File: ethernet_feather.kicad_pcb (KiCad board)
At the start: 4 copper layers, 100 parts, among them J1 JST PH 2 pin, J2 JST SH4 pin, J3 Molex 1051620001, J4 TC2030-NL, J5 USB_C_Receptacle_USB2.0, J6 RJ45_Abracon_ARJM11D7-114-AB-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, J7 2x2 header, Q1 Q_PMOS_DGS, U1 MIMXRT1051CVJ5B, U2 LP3982IMM-3.3, U3 MCP73831-2-OT, U4 W25Q32JVZP, U5 WE-TVS-82400102, U6 LAN8742A, U7 HSP061-4M10, Y1 32.768kHz, Y2 24MHz 6pF, Y3 25MHz

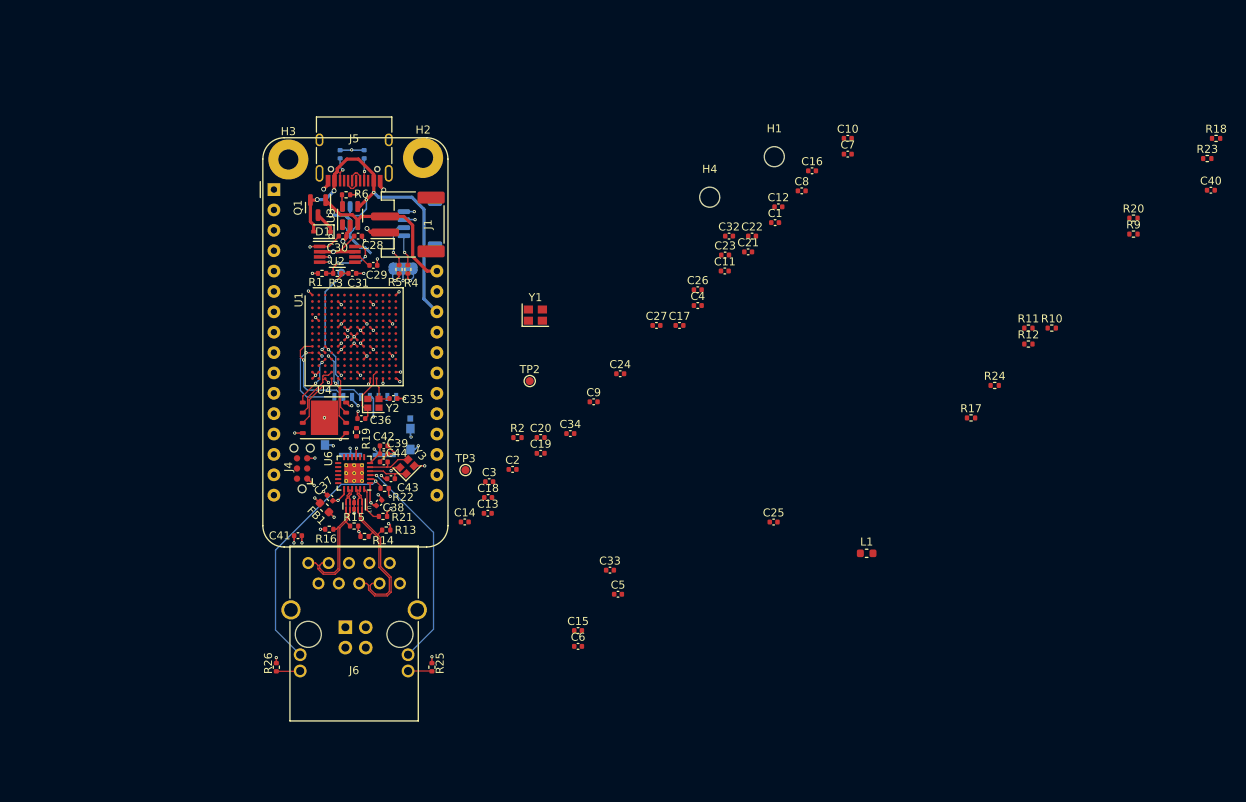
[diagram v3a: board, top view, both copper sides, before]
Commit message: Fix up mounting holes, route more flash and microSD
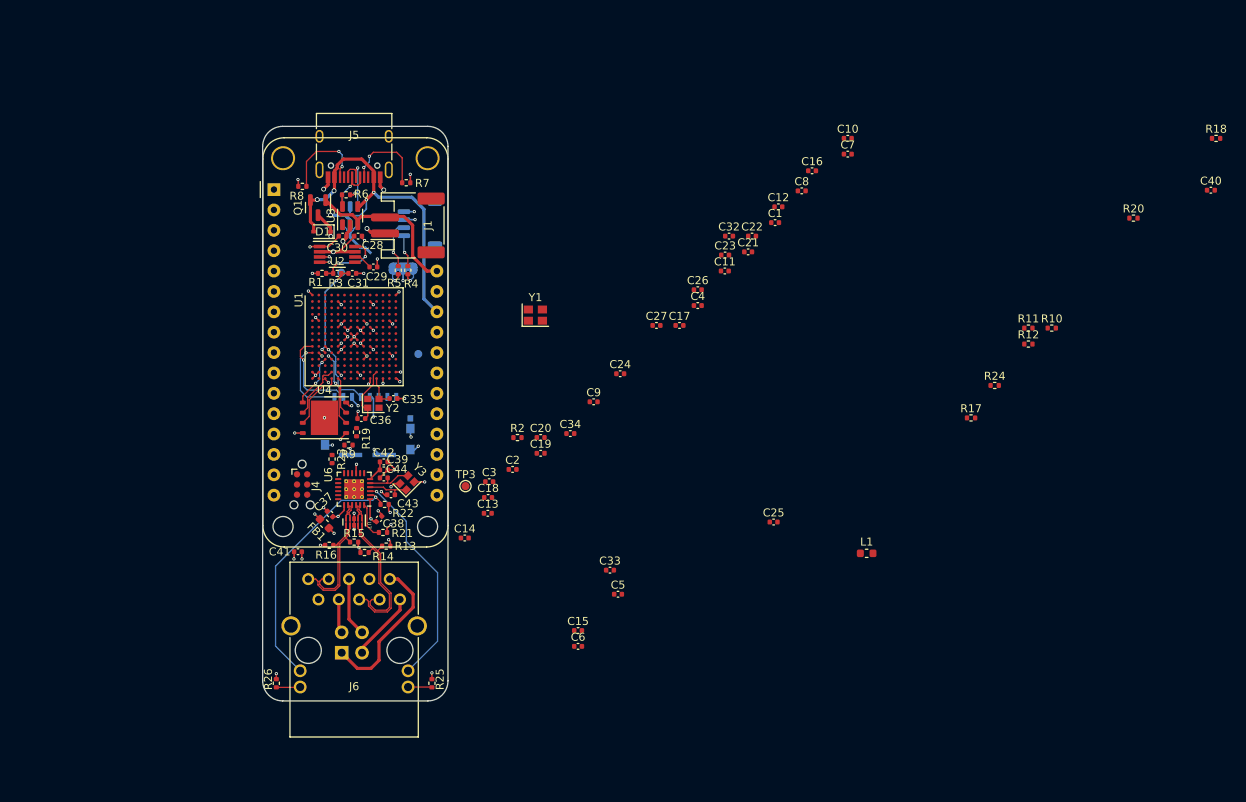
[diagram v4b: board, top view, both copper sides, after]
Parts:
- H1, H4: footprint MountingHole:MountingHole_2.5mm -> ethernet_feather:MountingHole_2.5mm_Small
- H2, H3: footprint MountingHole:MountingHole_2.5mm_Pad -> ethernet_feather:MountingHole_2.5mm_Pad_Small
- R7, R8: moved to F.Cu
- TP2: moved to B.Cu
- moved R23 115.4 mm to (107.2, 108.8), turned to -90 degrees
- moved R9 101.3 mm to (109.3, 107.1), turned to 180 degrees
- moved H1 76.7 mm to (101.1, 117.3)
- moved H4 54.1 mm to (119.2, 117.3)
- moved TP2 14.3 mm to (118.0, 95.8), turned to 180 degrees
- moved R7 6.34 mm to (116.5, 74.4), turned to 0 degrees
- moved R8 6.17 mm to (103.5, 74.8), turned to 180 degrees
- moved J7 3.21 mm to (108.5, 133.0), turned to -90 degrees
- moved C14 2.00 mm to (123.8, 118.7)
- moved C37 2.00 mm to (107.0, 115.7)
- moved C38 2.00 mm to (113.1, 116.3)
- moved C39 2.00 mm to (113.7, 110.2)
- moved C41 2.00 mm to (103.0, 120.4)
- moved C42 2.00 mm to (113.7, 109.2)
- moved C43 2.00 mm to (114.6, 113.3)
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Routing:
- net Net-(J6-Pad2): track 0.00 -> 19.6 mm
- net Net-(J6-Pad1): track 0.00 -> 8.60 mm
- net Net-(J5-PadB5): track 3.07 -> 11.1 mm, vias 1 -> 2
- net Net-(J5-PadA5): track 2.83 -> 10.6 mm, vias 1 -> 2
- net Net-(J6-Pad6): track 0.00 -> 7.31 mm
- net /USB_DIRECT_D+: track 2.47 -> 8.75 mm, vias 0 -> 1
- net /USB_DIRECT_D-: track 2.46 -> 6.85 mm, vias 0 -> 1
- net Net-(J6-Pad7): track 0.00 -> 4.25 mm
- net DCDC_GND: track 58.9 -> 57.2 mm
- net NVCC_EMC: track 21.9 -> 20.7 mm, vias 18 -> 17
- net VUSB: track 46.3 -> 46.8 mm
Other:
- board outline added: 23.1 x 71.6 mm

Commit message: Old work, I have no idea what this is
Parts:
- Y1: footprint Crystal:Crystal_SMD_2520-4Pin_2.5x2.0mm -> Crystal:Crystal_SMD_3215-2Pin_3.2x1.5mm
- moved C10 62.8 mm to (117.8, 101.3), turned to -90 degrees
- moved L1 61.5 mm to (117.1, 97.0), turned to 90 degrees
- moved C8 55.0 mm to (116.8, 100.3), turned to -90 degrees
- moved R19 50.2 mm to (76.7, 142.8)
- moved TP2 45.3 mm to (73.2, 88.7)
- moved R9 45.0 mm to (69.1, 127.3)
- moved C33 44.2 mm to (110.0, 92.1)
- moved J3 40.6 mm to (80.7, 78.0)
- moved C32 39.1 mm to (118.4, 88.5), turned to -90 degrees
- moved C26 35.7 mm to (118.4, 97.3), turned to 90 degrees
- moved C34 34.1 mm to (107.6, 88.3)
- moved C27 30.2 mm to (118.3, 99.5), turned to -90 degrees
- moved Y1 22.8 mm to (109.8, 89.5), turned to 90 degrees
- moved U4 16.0 mm to (114.4, 89.9)
- moved C36 14.7 mm to (107.0, 89.6)
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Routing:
- net Net-(J3-Pad7): track 11.9 -> 0.00 mm, vias 1 -> 0
- net Net-(C31-Pad1): track 12.3 -> 0.89 mm, vias 2 -> 0
- net Net-(J3-Pad8): track 10.4 -> 0.00 mm, vias 1 -> 0
- net Net-(J3-Pad5): track 9.05 -> 0.00 mm, vias 1 -> 0
- net Net-(C34-Pad2): track 0.00 -> 8.94 mm
- net Net-(U1-PadP5): track 4.68 -> 13.0 mm, vias 0 -> 2
- net VDD_SOC_IN: track 5.66 -> 12.6 mm, vias 5 -> 6
- net Net-(C33-Pad2): track 0.00 -> 6.96 mm
- net Net-(U1-PadL3): track 6.80 -> 11.6 mm, vias 2 -> 3
- net Net-(U1-PadP3): track 1.75 -> 5.39 mm, vias 2 -> 0
- net Net-(L1-Pad2): track 0.00 -> 3.46 mm
- net Net-(U1-PadP4): track 7.49 -> 4.79 mm
- net Net-(U1-PadL4): track 9.81 -> 11.5 mm
- net DCDC_GND: track 57.2 -> 58.3 mm, vias 51 -> 52
- net NVCC_EMC: track 20.7 -> 20.0 mm, vias 17 -> 15
